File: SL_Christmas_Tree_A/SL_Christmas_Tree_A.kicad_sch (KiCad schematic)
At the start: 60 parts, among them J101 5V, J102 GND, J201 5V, J202 GND

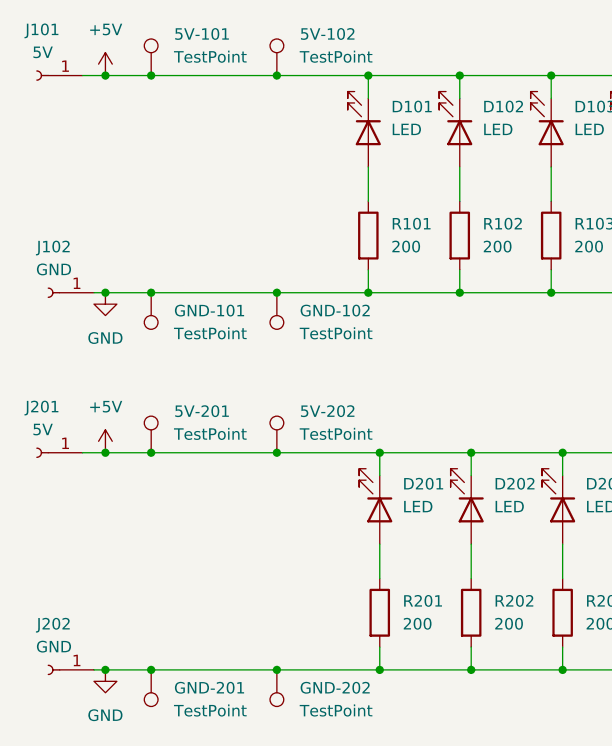
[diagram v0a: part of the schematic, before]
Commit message: fix swapped 5V / GND
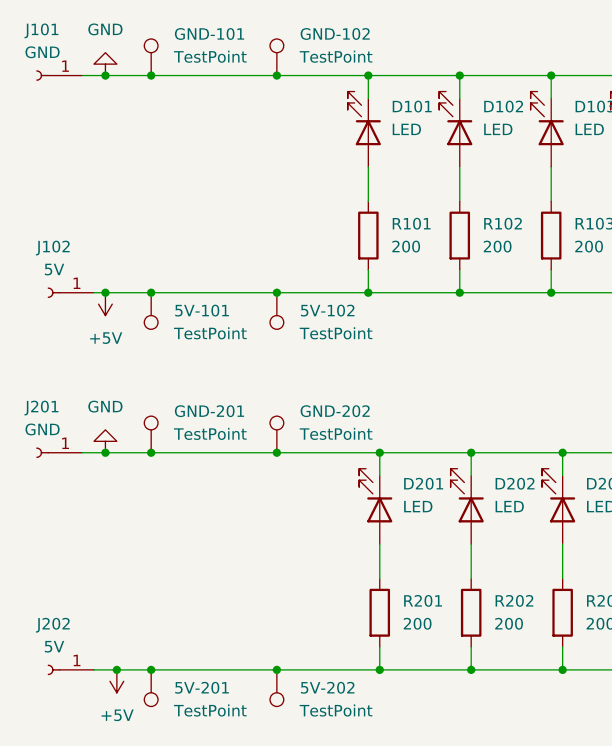
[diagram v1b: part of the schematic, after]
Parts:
- J101, J201: value 5V -> GND
- J102, J202: value GND -> 5V
- renumbered GND-101 to 5V-101, GND-102 to 5V-102, GND-201 to 5V-201, GND-202 to 5V-202, 5V-101 to GND-101, 5V-102 to GND-102, 5V-201 to GND-201, 5V-202 to GND-202
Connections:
- net +5V: now also 5V-101.1, 5V-102.1, 5V-201.1, 5V-202.1, J102.1 (Pin_1), J202.1 (Pin_1), R101.2, R102.2, R103.2, R104.2, R105.2, R106.2, R107.2, R108.2, R109.2, R110.2, R111.2, R112.2, R201.2, R202.2, R203.2, R204.2, R205.2, R206.2, R207.2, R208.2, R209.2, R210.2, R211.2, R212.2; no longer D101.1 (K), D102.1 (K), D103.1 (K), D104.1 (K), D105.1 (K), D106.1 (K), D107.1 (K), D108.1 (K), D109.1 (K), D110.1 (K), D111.1 (K), D112.1 (K), D201.1 (K), D202.1 (K), D203.1 (K), D204.1 (K), D205.1 (K), D206.1 (K), D207.1 (K), D208.1 (K), D209.1 (K), D210.1 (K), D211.1 (K), D212.1 (K), GND-101.1, GND-102.1, GND-201.1, GND-202.1, J101.1 (Pin_1), J201.1 (Pin_1)
- net GND: now also D101.1 (K), D102.1 (K), D103.1 (K), D104.1 (K), D105.1 (K), D106.1 (K), D107.1 (K), D108.1 (K), D109.1 (K), D110.1 (K), D111.1 (K), D112.1 (K), D201.1 (K), D202.1 (K), D203.1 (K), D204.1 (K), D205.1 (K), D206.1 (K), D207.1 (K), D208.1 (K), D209.1 (K), D210.1 (K), D211.1 (K), D212.1 (K), GND-101.1, GND-102.1, GND-201.1, GND-202.1, J101.1 (Pin_1), J201.1 (Pin_1); no longer 5V-101.1, 5V-102.1, 5V-201.1, 5V-202.1, J102.1 (Pin_1), J202.1 (Pin_1), R101.2, R102.2, R103.2, R104.2, R105.2, R106.2, R107.2, R108.2, R109.2, R110.2, R111.2, R112.2, R201.2, R202.2, R203.2, R204.2, R205.2, R206.2, R207.2, R208.2, R209.2, R210.2, R211.2, R212.2

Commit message: PCB A v2.0
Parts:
- removed D101, D102, D103, D104, D105, D106, D107, D108, D109, D110, D111, D112, D201, D202, D203, D204, D205, D206, D207, D208, D209, D210, D211, D212: LED, LED_SMD:LED_0807_Slow_Flashing_Diode, symbol Device:LED
- removed R101, R102, R103, R104, R105, R106, R107, R108, R109, R110, R111, R112, R201, R202, R203, R204, R205, R206, R207, R208, R209, R210, R211, R212: 200, Resistor_SMD:R_0805_2012Metric_Pad1.20x1.40mm_HandSolder, symbol Device:R
- added C101, C102, C103, C104, C105, C106, C107, C108, C109, C110, C111, C112, C113, C201, C202, C203, C204, C205, C206, C207, C208, C209, C210, C211, C212, C213: 100nF, Capacitor_SMD:C_0805_2012Metric_Pad1.18x1.45mm_HandSolder, symbol Device:C
- added D101, D102, D103, D104, D105, D106, D108, D109, D110, D111, D112, D113, D201, D202, D203, D204, D205, D206, D208, D209, D210, D211, D212, D213: SK6812MINI, parts:LED_SK6812MINI_PLCC4_3.5x3.5mm_P1.75mm, symbol LED:SK6812MINI
- added D107, D207: SK6812 4020, parts:LED_SK6812_4020, symbol LED_SK6812_4020:SK6812_4020
- added DIN101, DIN202, DOUT101, DOUT201: TestPoint, TestPoint:TestPoint_Pad_3.0x3.0mm, symbol Connector:TestPoint
- added J103: DATA, Connector_Wire:SolderWire-1.5sqmm_1x01_D1.7mm_OD3.9mm, symbol Connector:Conn_01x01_Female
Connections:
- net +5V: now also C101.2, C102.2, C103.2, C104.2, C105.2, C106.2, C107.1, C108.2, C109.2, C110.2, C111.2, C112.2, C113.2, C201.2, C202.2, C203.2, C204.2, C205.2, C206.2, C207.1, C208.2, C209.2, C210.2, C211.2, C212.2, C213.2, D101.4 (VDD), D102.4 (VDD), D103.4 (VDD), D104.4 (VDD), D105.4 (VDD), D106.4 (VDD), D107.2 (VDD), D108.4 (VDD), D109.4 (VDD), D110.4 (VDD), D111.4 (VDD), D112.4 (VDD), D113.4 (VDD), D201.4 (VDD), D202.4 (VDD), D203.4 (VDD), D204.4 (VDD), D205.4 (VDD), D206.4 (VDD), D207.2 (VDD), D208.4 (VDD), D209.4 (VDD), D210.4 (VDD), D211.4 (VDD), D212.4 (VDD), D213.4 (VDD)
- net GND: now also C101.1, C102.1, C103.1, C104.1, C105.1, C106.1, C107.2, C108.1, C109.1, C110.1, C111.1, C112.1, C113.1, C201.1, C202.1, C203.1, C204.1, C205.1, C206.1, C207.2, C208.1, C209.1, C210.1, C211.1, C212.1, C213.1, D101.2 (VSS), D102.2 (VSS), D103.2 (VSS), D104.2 (VSS), D105.2 (VSS), D106.2 (VSS), D107.4 (GND), D108.2 (VSS), D109.2 (VSS), D110.2 (VSS), D111.2 (VSS), D112.2 (VSS), D113.2 (VSS), D201.2 (VSS), D202.2 (VSS), D203.2 (VSS), D204.2 (VSS), D205.2 (VSS), D206.2 (VSS), D207.4 (GND), D208.2 (VSS), D209.2 (VSS), D210.2 (VSS), D211.2 (VSS), D212.2 (VSS), D213.2 (VSS)
- new net: D212.1 (DOUT), D213.3 (DIN)
- new net: D103.1 (DOUT), D104.3 (DIN)
- new net: D102.1 (DOUT), D103.3 (DIN)
- new net: D101.1 (DOUT), D102.3 (DIN)
- new net: D101.3 (DIN), J103.1 (Pin_1)
- new net: D208.3 (DIN), DIN202.1
- new net: D112.1 (DOUT), D113.3 (DIN)
- new net: D204.1 (DOUT), D205.3 (DIN)
- new net: D203.1 (DOUT), D204.3 (DIN)
- new net: D108.1 (DOUT), D109.3 (DIN)
- new net: D108.3 (DIN), DIN101.1
- new net: D210.1 (DOUT), D211.3 (DIN)
- new net: D209.1 (DOUT), D210.3 (DIN)
- new net: D211.1 (DOUT), D212.3 (DIN)
- new net: D111.1 (DOUT), D112.3 (DIN)
- new net: D110.1 (DOUT), D111.3 (DIN)
- new net: D208.1 (DOUT), D209.3 (DIN)
- new net: D104.1 (DOUT), D105.3 (DIN)
- new net: D202.1 (DOUT), D203.3 (DIN)
- new net: D105.1 (DOUT), D106.3 (DIN)
- new net: D206.1 (DOUT), D207.1 (DIN)
- new net: D207.3 (DOUT), DOUT201.1
- new net: D201.1 (DOUT), D202.3 (DIN)
- new net: D205.1 (DOUT), D206.3 (DIN)
- new net: D109.1 (DOUT), D110.3 (DIN)
- new net: D106.1 (DOUT), D107.1 (DIN)
- new net: D107.3 (DOUT), DOUT101.1
- new net Conn_A-OUT_B-IN: D113.1 (DOUT), D201.3 (DIN)
- no-connect marks 0 -> 1
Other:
- note added: "Side A"
- note added: "Side B"
- company: (none) -> Sternenlabor e.V.
- title: (none) -> Christmas Tree 2024
- moved on the sheet: 5V-101, 5V-102, GND-101, GND-102, J101, J102

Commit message: small Footprint changes and prepared "Side B" for placing parts
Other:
- title: Christmas Tree 2024 -> Christmas Tree 2024 - Side A
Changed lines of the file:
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@@
 	(paper "A3")
 	(title_block
-		(title "Christmas Tree 2024")
+		(title "Christmas Tree 2024 - Side A")
 		(date "2024-10-15")
 		(rev "2.0")

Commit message: WIP v2.1
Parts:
- added J2: DS, Connector_Wire:SolderWire-1.5sqmm_1x01_D1.7mm_OD3.9mm, symbol Connector:Conn_01x01_Female
- J103: value DATA -> DT
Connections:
- net at D207.1 (DIN): now also D107.3 (DOUT); no longer D206.1 (DOUT)
- net at D207.3 (DOUT): no longer DOUT201.1
- net at D107.1 (DIN): now also J2.1 (Pin_1); no longer D106.1 (DOUT)
- net at DOUT101.1: now also D106.1 (DOUT); no longer D107.3 (DOUT)
- new net: D206.1 (DOUT), DOUT201.1
- no-connect marks 1 -> 2
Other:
- note added: "Starlight"
- moved on the sheet: 5V-101, 5V-102, 5V-201, 5V-202, C101, C102, C103, C104, C105, C106, C107, C108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
